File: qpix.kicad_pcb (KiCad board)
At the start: 4 copper layers, 82.6 x 94.6 mm, 107 parts, among them J1 Conn_01x32, J11 Conn_Coaxial_Power, J13 DigReset, J2 Conn_01x09, J3 Conn_02x03, J4 Conn_02x03, J5 SPI, J6 Conn_02x03, J7 Conn_Coaxial, J8 Conn_02x03, J9 Conn_Coaxial_Power, Q1 Q_NMOS_GSD, Q2 Q_NMOS_GSD, Q3 Q_NMOS_GSD, Q4 Q_NMOS_GSD, U1 qpix_digital, U2 TPS73101DBV, U3 9DMV0141AKILF, U4 DS90C401M_NOPB

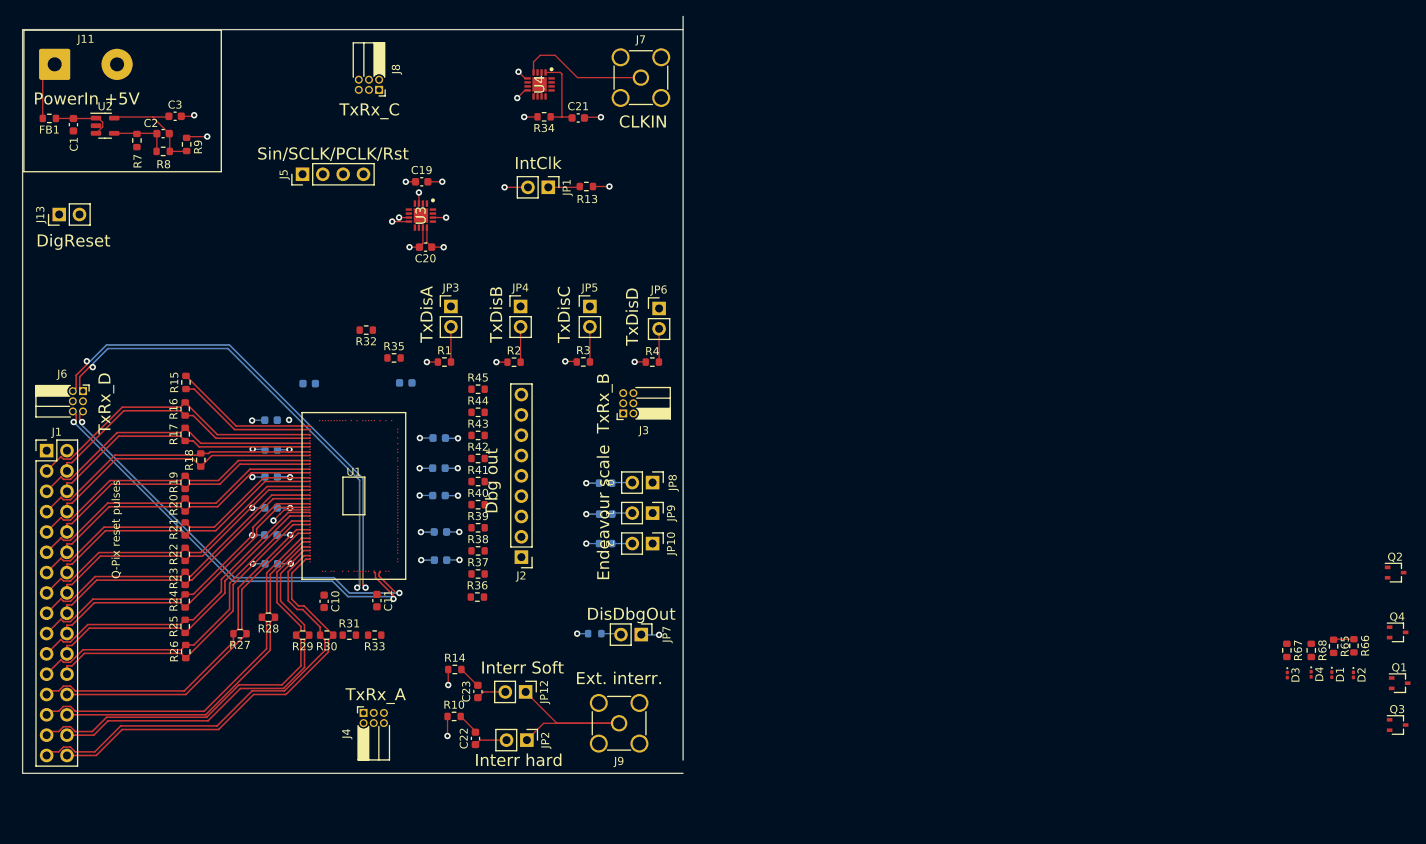
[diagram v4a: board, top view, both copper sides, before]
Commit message: the board is fully routed for the first time
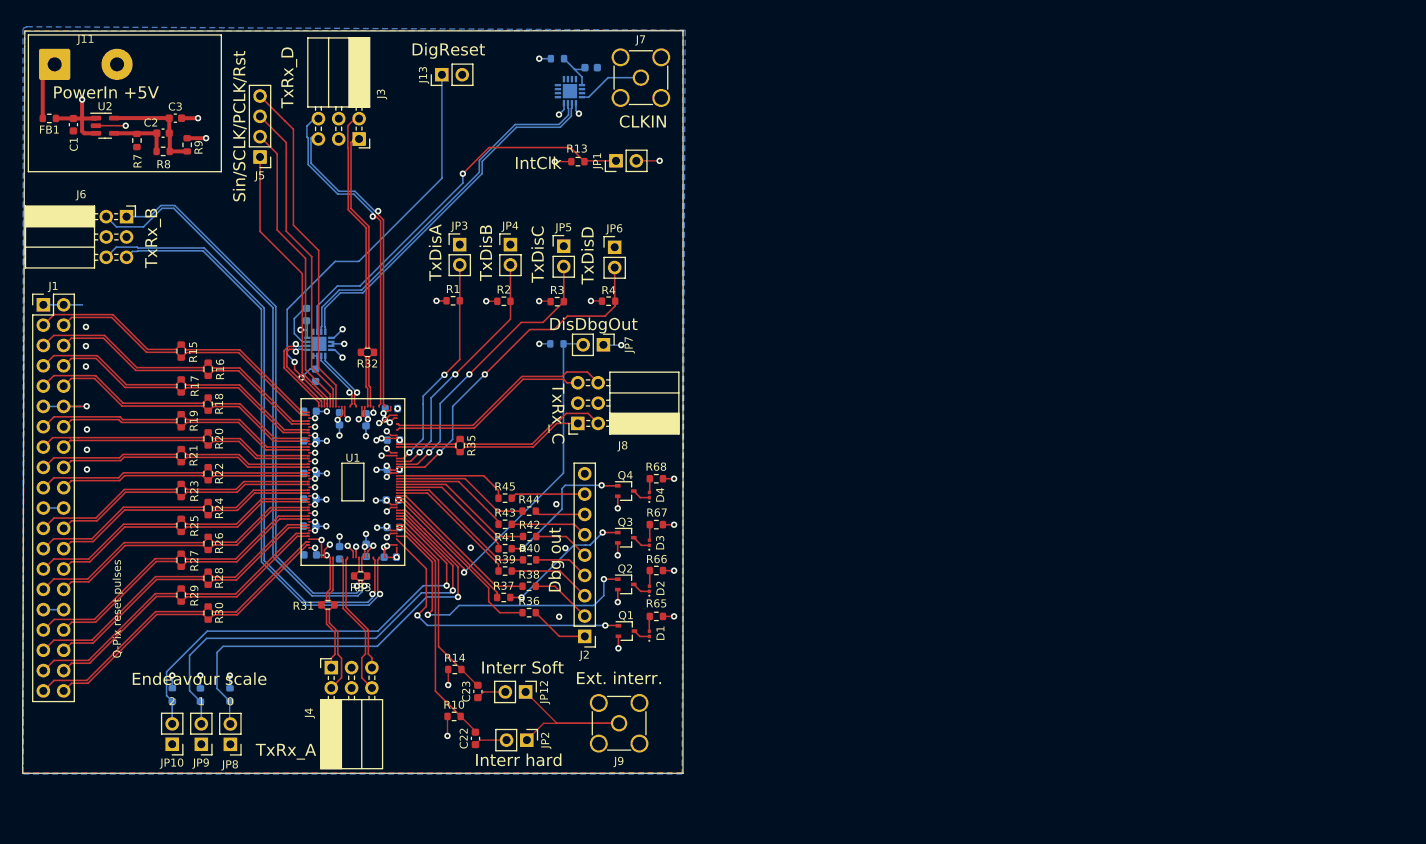
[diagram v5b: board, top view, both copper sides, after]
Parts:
- added C24: C, Capacitor_SMD:C_0603_1608Metric, B.Cu at (141.2, 115.2)
- C10, C11, C19, C20, C21, R34, U3, U4: moved to B.Cu
- C13, C14, C15, C16: value C -> locked
- J1: value Conn_01x32 -> Conn_01x40; footprint Connector_PinHeader_2.54mm:PinHeader_2x16_P2.54mm_Vertical -> Connector_PinHeader_2.54mm:PinHeader_2x20_P2.54mm_Vertical
- J3, J4, J6, J8: footprint Connector_PinSocket_1.27mm:PinSocket_2x03_P1.27mm_Horizontal -> Connector_PinSocket_2.54mm:PinSocket_2x03_P2.54mm_Horizontal
- moved Q3 99.3 mm to (170.7, 112.8)
- moved Q4 98.1 mm to (170.7, 107.0)
- moved Q1 96.9 mm to (170.7, 124.5)
- moved Q2 96.2 mm to (170.7, 118.6)
- moved D2 88.7 mm to (173.6, 119.2), turned to 90 degrees
- moved R66 87.7 mm to (174.5, 116.9), turned to 180 degrees
- moved D4 85.7 mm to (173.6, 107.5), turned to 90 degrees
- moved D1 85.5 mm to (173.6, 124.8), turned to 90 degrees
- moved R65 84.7 mm to (174.5, 122.6), turned to 180 degrees
- moved R68 84.6 mm to (174.5, 105.4), turned to 180 degrees
- moved D3 81.4 mm to (173.6, 113.4), turned to 90 degrees
- moved R67 80.4 mm to (174.5, 111.2), turned to 180 degrees
- moved JP10 65.1 mm to (114.0, 138.6), turned to 180 degrees
- moved JP9 63.4 mm to (117.6, 138.6), turned to 180 degrees
- moved JP8 62.1 mm to (121.2, 138.6), turned to 180 degrees
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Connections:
- net Net-(J3-Pad1) renamed /DatainD_P
- net Net-(J8-Pad1) renamed /DatainC_P
- J1 pad 1: Reset15_P -> GND
- J1 pad 10: Reset11_N -> Reset12_N
- J1 pad 11: Reset10_P -> GND
- J1 pad 12: Reset10_N -> GND
- J1 pad 13: Reset9_P -> Reset11_P
- J1 pad 14: Reset9_N -> Reset11_N
- J1 pad 15: Reset8_P -> Reset10_P
- J1 pad 16: Reset8_N -> Reset10_N
- J1 pad 17: Reset7_P -> Reset9_P
- J1 pad 18: Reset7_N -> Reset9_N
- J1 pad 19: Reset6_P -> Reset8_P
- J1 pad 2: Reset15_N -> GND
- J1 pad 20: Reset6_N -> Reset8_N
- J1 pad 21: Reset5_P -> GND
- J1 pad 22: Reset5_N -> GND
- J1 pad 23: Reset4_P -> Reset7_P
- J1 pad 24: Reset4_N -> Reset7_N
- J1 pad 25: Reset3_P -> Reset6_P
- J1 pad 26: Reset3_N -> Reset6_N
- J1 pad 27: Reset2_P -> Reset5_P
- J1 pad 28: Reset2_N -> Reset5_N
- J1 pad 29: Reset1_P -> Reset4_P
- J1 pad 3: Reset14_P -> Reset15_P
- J1 pad 30: Reset1_N -> Reset4_N
- J1 pad 31: Reset0_P -> GND
- J1 pad 32: Reset0_N -> GND
- J1 pad 4: Reset14_N -> Reset15_N
- J1 pad 5: Reset13_P -> Reset14_P
- J1 pad 6: Reset13_N -> Reset14_N
- J1 pad 7: Reset12_P -> Reset13_P
- J1 pad 8: Reset12_N -> Reset13_N
- J1 pad 9: Reset11_P -> Reset12_P
- J3 pad 2: Net-(J3-Pad2) -> /DatainD_N
- J3 pad 5: Net-(J3-Pad5) -> /DataoutD_P
- J3 pad 6: Net-(J3-Pad6) -> /DataoutD_N
- J4 pad 2: /DatoutA_P -> /DatinA_N
- J4 pad 5: /DatoutA_N -> /DatoutA_P
- J4 pad 6: /DatinA_N -> /DatoutA_N
- J8 pad 2: Net-(J8-Pad2) -> /DatainC_N
- J8 pad 5: Net-(J8-Pad5) -> /DataoutC_P
- J8 pad 6: Net-(J8-Pad6) -> /DataoutC_N
- R32 pad 2: Net-(J3-Pad6) -> /DatainD_N
- R35 pad 1: Net-(J8-Pad6) -> /DatainC_N
- U1 pad 101: Net-(J8-Pad2) -> /DataoutC_P
- U1 pad 102: Net-(J8-Pad5) -> /DataoutC_N
- U1 pad 106: Net-(J3-Pad2) -> /DataoutD_P
- U1 pad 107: Net-(J3-Pad5) -> /DataoutD_N
- U1 pad 110: Net-(J3-Pad6) -> /DatainD_N
- U1 pad 117: VDD -> unconnected-(U1-Pad117)
- U1 pad 98: Net-(J8-Pad6) -> /DatainC_N
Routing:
- net EndeavorScale_1: track 2.55 -> 58.3 mm, vias 0 -> 1
- net EndeavorScale_2: track 2.51 -> 57.7 mm, vias 0 -> 1
- net EndeavorScale_0: track 2.54 -> 56.5 mm, vias 0 -> 1
- net Net-(J13-Pad1): track 0.00 -> 53.2 mm, vias 0 -> 1
- net /clkmux/DO-: track 0.00 -> 46.3 mm
- net /clkmux/DO+: track 0.00 -> 46.3 mm
- net disableDbgOut: track 2.50 -> 48.1 mm, vias 0 -> 1
- net /clkmux/SEL_AB: track 5.50 -> 50.1 mm
- net /SR_reset: track 0.00 -> 42.8 mm
- net /DataoutD_N: track 0.00 -> 42.5 mm, vias 0 -> 1
- net /PCLK: track 0.00 -> 40.1 mm
- net /DataoutD_P: track 0.00 -> 39.9 mm, vias 0 -> 1
- net dbgDataValid: track 0.00 -> 39.4 mm, vias 0 -> 2
- net TxRxDisable_3: track 4.17 -> 42.9 mm, vias 0 -> 2
- net /DatainD_N: track 0.00 -> 38.7 mm
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- added copper zone on In2.Cu, net +5V
- added copper zone on B.Cu, net GND
- added copper zone on F.Cu, net GND
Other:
- board size 82.6 x 94.6 mm -> 82.6 x 92.8 mm

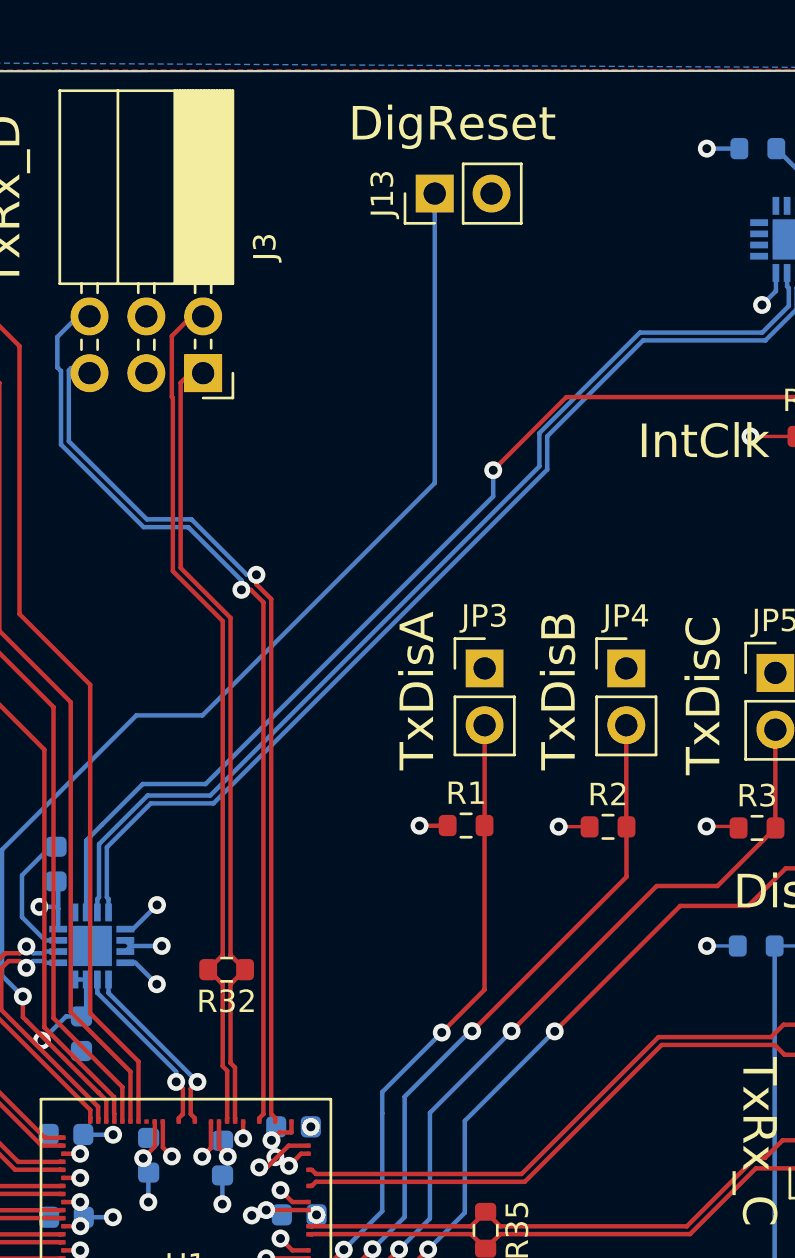
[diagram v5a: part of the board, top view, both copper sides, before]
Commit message: connect VC DAC reference voltage to the pin header
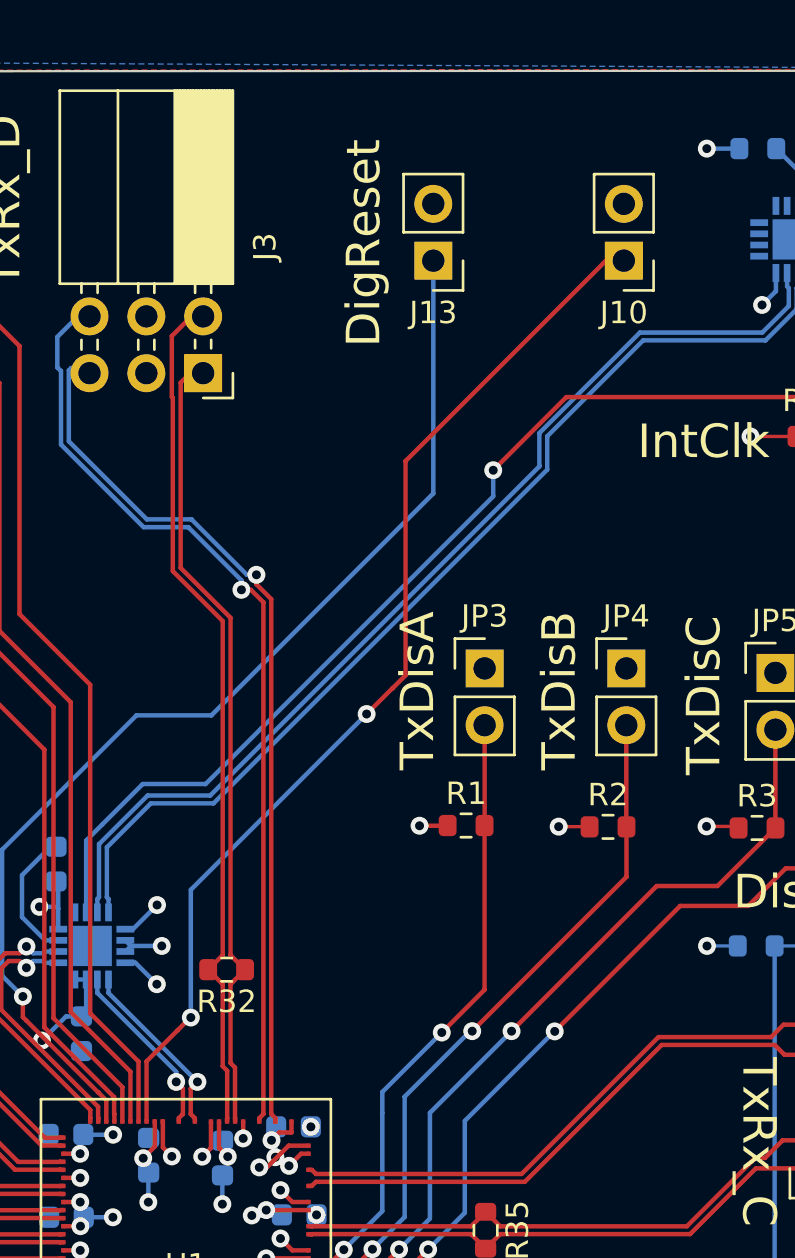
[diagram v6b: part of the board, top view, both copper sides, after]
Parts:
- added J10: VC, Connector_PinHeader_2.54mm:PinHeader_1x02_P2.54mm_Vertical, F.Cu at (156.1, 57.9)
- moved J13 3.00 mm to (147.6, 57.9), turned to 180 degrees
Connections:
- U1 pad 117: unconnected-(U1-Pad117) -> Net-(U1-Pad117)
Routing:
- net Net-(U1-Pad117): track 0.00 -> 47.8 mm, vias 0 -> 2
- net Net-(J13-Pad1): track 53.2 -> 50.4 mm
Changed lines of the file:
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@@
   (net 106 "/clkmux/DO-")
   (net 107 "/clkmux/SEL_AB")
-  (net 108 "unconnected-(U1-Pad117)")
+  (net 108 "Net-(U1-Pad117)")
   (net 109 "/DatainC_N")
   (net 110 "/DataoutC_N")
@@
       (net 3 "VDD") (pinfunction "VDD") (pintype "power_in"))
     (pad "117" smd rect (at -1.76 -9.42) (size 0.2 0.2) (layers "F.Cu" "F.Paste" "F.Mask")
-      (net 108 "unconnected-(U1-Pad117)") (pinfunction "VC") (pintype "power_in+no_connect"))
+      (net 108 "Net-(U1-Pad117)") (pinfunction "VC") (pintype "output"))
     (pad "118" smd rect (at -2.12 -9.42) (size 0.2 0.2) (layers "F.Cu" "F.Paste" "F.Mask")
       (net 67 "/SR_reset") (pinfunction "SR_reset") (pintype "input"))
@@
   )
   (footprint "Connector_PinHeader_2.54mm:PinHeader_1x02_P2.54mm_Vertical" (layer "F.Cu")
-    (at 147.665 54.92 90)
+    (at 147.6 57.92 180)
     (descr "Through hole straight pin header, 1x02, 2.54mm pitch, single row")
     (tags "Through hole pin header THT 1x02 2.54mm single row")
@@
     (property "Sheetname" "")
     (attr through_hole)
-    (fp_text reference "J13" (at 0 -2.33 90) (layer "F.SilkS")
+    (fp_text reference "J13" (at 0 -2.33) (layer "F.SilkS")
       (effects (font (size 1 1) (thickness 0.15)))
     )
-    (fp_text value "DigReset" (at 0 4.87 90) (layer "F.Fab")
+    (fp_text value "DigReset" (at 0 4.87) (layer "F.Fab")
       (effects (font (size 1 1) (thickness 0.15)))
     )
-    (fp_text user "${REFERENCE}" (at 0 1.27) (layer "F.Fab")
+    (fp_text user "${REFERENCE}" (at 0 1.27 90) (layer "F.Fab")
       (effects (font (size 1 1) (thickness 0.15)))
     )
@@
     (fp_line (start 1.27 3.81) (end -1.27 3.81) (layer "F.Fab") (width 0.1))
     (fp_line (start -1.27 3.81) (end -1.27 -0.635) (layer "F.Fab") (width 0.1))
-    (pad "1" thru_hole rect (at 0 0 90) (size 1.7 1.7) (drill 1) (layers *.Cu *.Mask)
+    (pad "1" thru_hole rect (at 0 0 180) (size 1.7 1.7) (drill 1) (layers *.Cu *.Mask)
       (net 68 "Net-(J13-Pad1)") (pinfunction "Pin_1") (pintype "passive"))
-    (pad "2" thru_hole oval (at 0 2.54 90) (size 1.7 1.7) (drill 1) (layers *.Cu *.Mask)
+    (pad "2" thru_hole oval (at 0 2.54 180) (size 1.7 1.7) (drill 1) (layers *.Cu *.Mask)
       (net 2 "GND") (pinfunction "Pin_2") (pintype "passive"))
     (model "${KICAD6_3DMODEL_DIR}/Connector_PinHeader_2.54mm.3dshapes/PinHeader_1x02_P2.54mm_Vertical.wrl"
@@
     )
   )
+  (footprint "Connector_PinHeader_2.54mm:PinHeader_1x02_P2.54mm_Vertical" (layer "F.Cu")
+    (at 156.12 57.92 180)
+    (descr "Through hole straight pin header, 1x02, 2.54mm pitch, single row")
+    (tags "Through hole pin header THT 1x02 2.54mm single row")
+    (property "Sheetfile" "qpix.kicad_sch")
+    (property "Sheetname" "")
+    (attr through_hole)
+    (fp_text reference "J10" (at 0 -2.33) (layer "F.SilkS")
+      (effects (font (size 1 1) (thickness 0.15)))
+    )
+    (fp_text value "VC" (at 0 4.87) (layer "F.Fab")
+      (effects (font (size 1 1) (thickness 0.15)))
+    )
+    (fp_text user "${REFERENCE}" (at 0 1.27 90) (layer "F.Fab")
+      (effects (font (size 1 1) (thickness 0.15)))
+    )
+    (fp_line (start -1.33 0) (end -1.33 -1.33) (layer "F.SilkS") (width 0.12))
+    (fp_line (start -1.33 1.27) (end 1.33 1.27) (layer "F.SilkS") (width 0.12))
+    (fp_line (start 1.33 1.27) (end 1.33 3.87) (layer "F.SilkS") (width 0.12))
+    (fp_line (start -1.33 3.87) (end 1.33 3.87) (layer "F.SilkS") (width 0.12))
+    (fp_line (start -1.33 -1.33) (end 0 -1.33) (layer "F.SilkS") (width 0.12))
+    (fp_line (start -1.33 1.27) (end -1.33 3.87) (layer "F.SilkS") (width 0.12))
+    (fp_line (start 1.8 4.35) (end 1.8 -1.8) (layer "F.CrtYd") (width 0.05))
+    (fp_line (start -1.8 4.35) (end 1.8 4.35) (layer "F.CrtYd") (width 0.05))
+    (fp_line (start -1.8 -1.8) (end -1.8 4.35) (layer "F.CrtYd") (width 0.05))
+    (fp_line (start 1.8 -1.8) (end -1.8 -1.8) (layer "F.CrtYd") (width 0.05))
+    (fp_line (start 1.27 -1.27) (end 1.27 3.81) (layer "F.Fab") (width 0.1))
+    (fp_line (start 1.27 3.81) (end -1.27 3.81) (layer "F.Fab") (width 0.1))
+    (fp_line (start -1.27 3.81) (end -1.27 -0.635) (layer "F.Fab") (width 0.1))
+    (fp_line (start -0.635 -1.27) (end 1.27 -1.27) (layer "F.Fab") (width 0.1))
+    (fp_line (start -1.27 -0.635) (end -0.635 -1.27) (layer "F.Fab") (width 0.1))
+    (pad "1" thru_hole rect (at 0 0 180) (size 1.7 1.7) (drill 1) (layers *.Cu *.Mask)
+      (net 108 "Net-(U1-Pad117)") (pinfunction "Pin_1") (pintype "passive"))
+    (pad "2" thru_hole oval (at 0 2.54 180) (size 1.7 1.7) (drill 1) (layers *.Cu *.Mask)
+      (net 2 "GND") (pinfunction "Pin_2") (pintype "passive"))
+    (model "${KICAD6_3DMODEL_DIR}/Connector_PinHeader_2.54mm.3dshapes/PinHeader_1x02_P2.54mm_Vertical.wrl"
+      (offset (xyz 0 0 0))
+      (scale (xyz 1 1 1))
+      (rotate (xyz 0 0 0))
+    )
+  )
   (footprint "Resistor_SMD:R_0603_1608Metric" (layer "F.Cu")
     (at 174.47 105.416668 180)
@@
     (effects (font (size 1.5 1.5) (thickness 0.3)))
   )
-  (gr_text "DigReset" (at 148.45 51.81) (layer "F.SilkS")
+  (gr_text "DigReset" (at 144.49 57.135 90) (layer "F.SilkS")
     (effects (font (size 1.5 1.5) (thickness 0.3)))
   )
@@
   (via (at 129.25 90.82) (size 0.8) (drill 0.4) (layers "F.Cu" "B.Cu") (net 68))
   (segment (start 128.32 89.89) (end 128.32 84.257319) (width 0.2) (layer "B.Cu") (net 68))
+  (segment (start 134.327319 78.25) (end 137.68 78.25) (width 0.2) (layer "B.Cu") (net 68))
   (segment (start 129.25 90.82) (end 128.32 89.89) (width 0.2) (layer "B.Cu") (net 68))
-  (segment (start 147.665 67.865) (end 147.665 54.92) (width 0.2) (layer "B.Cu") (net 68))
-  (segment (start 137.28 78.25) (end 147.665 67.865) (width 0.2) (layer "B.Cu") (net 68))
   (segment (start 128.32 84.257319) (end 134.327319 78.25) (width 0.2) (layer "B.Cu") (net 68))
-  (segment (start 134.327319 78.25) (end 137.28 78.25) (width 0.2) (layer "B.Cu") (net 68))
+  (segment (start 147.6 68.33) (end 147.6 57.92) (width 0.2) (layer "B.Cu") (net 68))
+  (segment (start 137.68 78.25) (end 147.6 68.33) (width 0.2) (layer "B.Cu") (net 68))
   (segment (start 142.735026 108.29) (end 153.51 119.064974) (width 0.2) (layer "F.Cu") (net 69))
   (segment (start 142.02 108.29) (end 142.735026 108.29) (width 0.2) (layer "F.Cu") (net 69))
@@
   (segment (start 137.4 81.32) (end 137.42 81.32) (width 0.2) (layer "B.Cu") (net 107))
   (segment (start 132.08 83.85) (end 132.79 83.14) (width 0.2) (layer "B.Cu") (net 107))
+  (segment (start 145.77 77.04) (end 145.78 77.04) (width 0.2) (layer "F.Cu") (net 108))
+  (segment (start 155.32 57.92) (end 156.12 57.92) (width 0.2) (layer "F.Cu") (net 108))
+  (segment (start 136.74 91.76) (end 136.76 91.76) (width 0.2) (layer "F.Cu") (net 108))
+  (segment (start 134.78 93.72) (end 136.17 92.33) (width 0.2) (layer "F.Cu") (net 108))
+  (segment (start 134.78 96.41) (end 134.78 93.72) (width 0.2) (layer "F.Cu") (net 108))
+  (segment (start 146.36 66.88) (end 155.32 57.92) (width 0.2) (layer "F.Cu") (net 108))
+  (segment (start 146.36 76.46) (end 146.36 66.88) (width 0.2) (layer "F.Cu") (net 108))
+  (segment (start 144.62 78.19) (end 145.77 77.04) (width 0.2) (layer "F.Cu") (net 108))
+  (segment (start 145.78 77.04) (end 146.36 76.46) (width 0.2) (layer "F.Cu") (net 108))
+  (segment (start 136.17 92.33) (end 136.74 91.76) (width 0.2) (layer "F.Cu") (net 108))
+  (via (at 136.76 91.76) (size 0.8) (drill 0.4) (layers "F.Cu" "B.Cu") (net 108))
+  (via (at 144.62 78.19) (size 0.8) (drill 0.4) (layers "F.Cu" "B.Cu") (net 108))
+  (segment (start 136.76 86.05) (end 144.62 78.19) (width 0.2) (layer "B.Cu") (net 108))
+  (segment (start 136.76 91.76) (end 136.76 86.05) (width 0.2) (layer "B.Cu") (net 108))
   (segment (start 161.992512 98.04) (end 162.43 98.04) (width 0.2) (layer "F.Cu") (net 109))
   (segment (start 158.937512 101.095) (end 161.992512 98.04) (width 0.2) (layer "F.Cu") (net 109))
